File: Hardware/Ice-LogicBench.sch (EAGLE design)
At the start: 106 parts, among them IC1 S27KL0641DABHV020, IC2 S26KL128SDABHI020, IC3 USBLC6-2SC6, IC4 ICE40HX4K-BG121, IC5 FUSB302MPX, IC6 USBLC6-2SC6, J2 QWIIC_RIGHT_ANGLE, Y3 12MZ

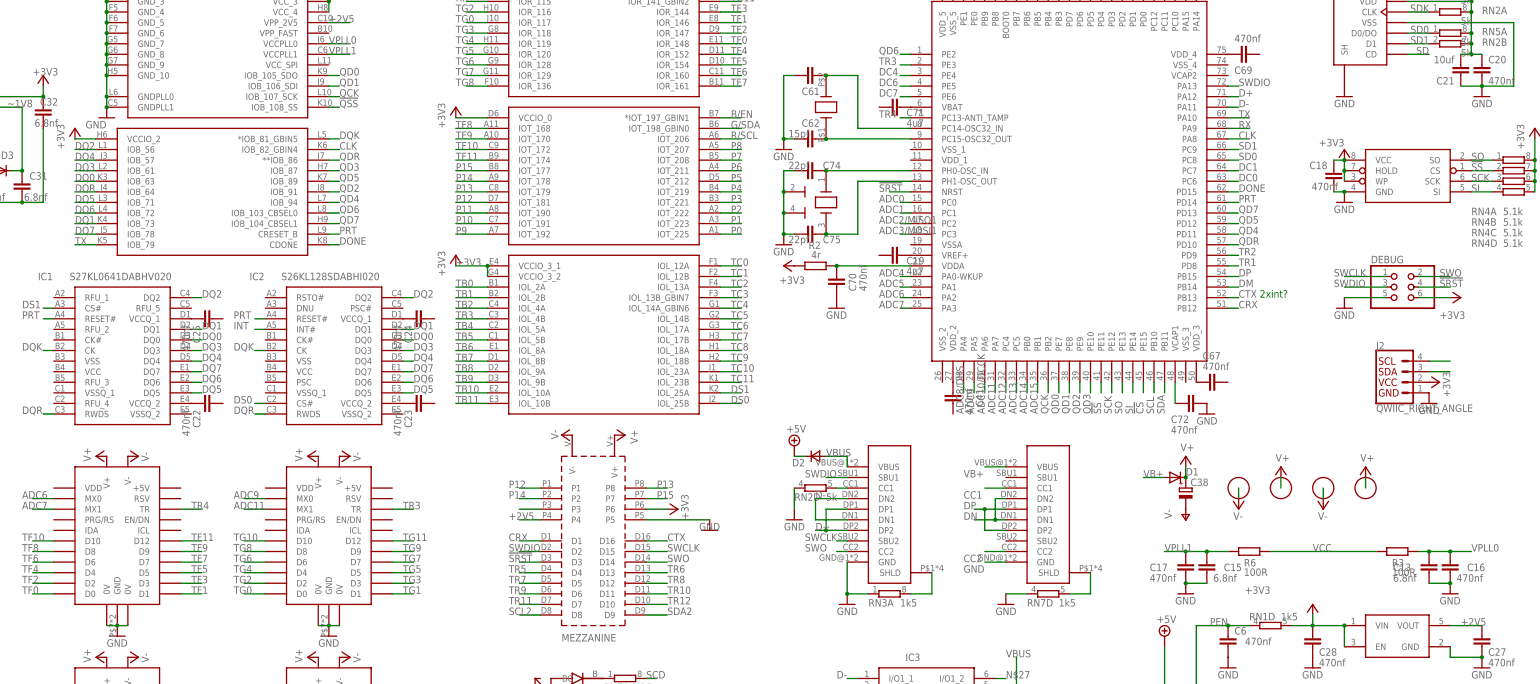
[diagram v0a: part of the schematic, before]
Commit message: Juggled some pins to improve IO frm @tnt suggestion
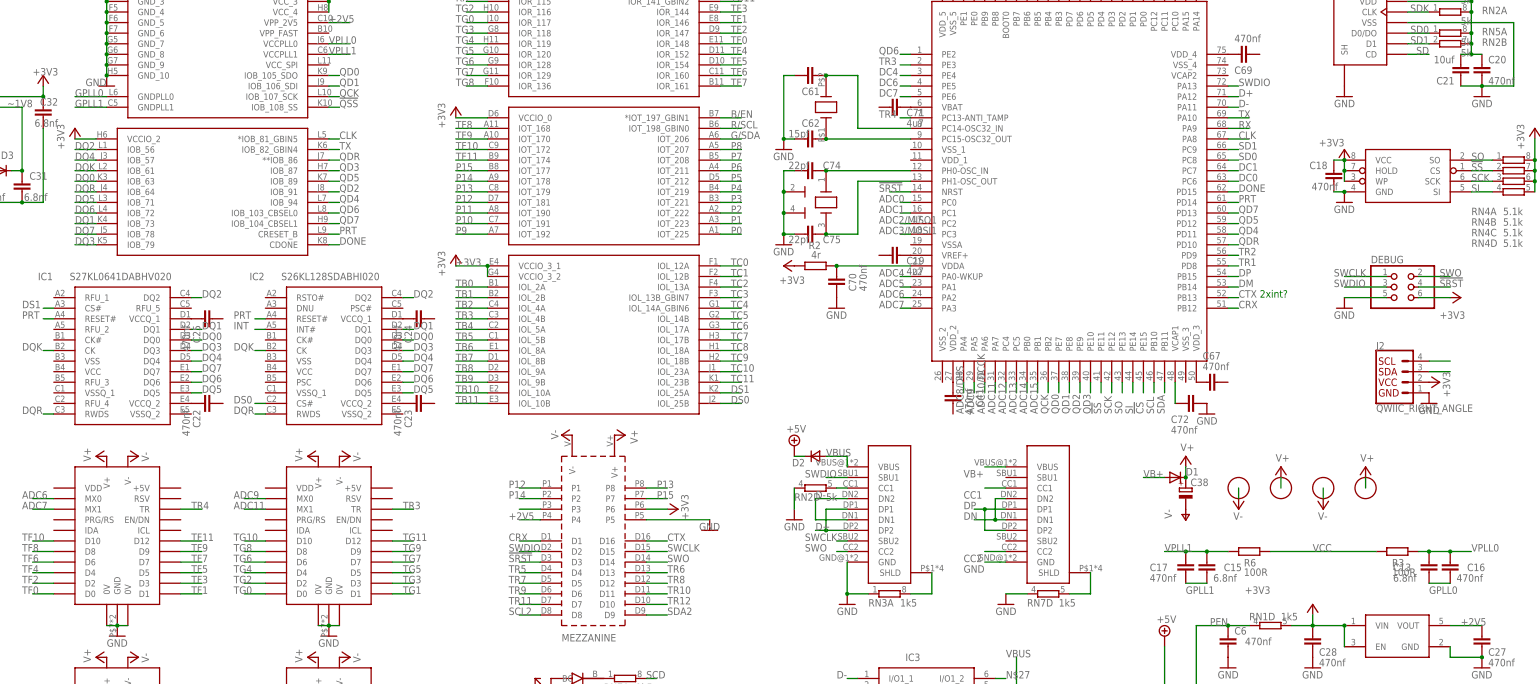
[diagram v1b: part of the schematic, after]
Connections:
- new net GPLL0: C13.1, C16.1, IC4.GNDPLL0
- new net GPLL1: C15.1, C17.1, IC4.GNDPLL1
- net CLK: now also IC4.*IOB_81_GBIN5; no longer IC4.IOB_82_GBIN4
- net DQ3: now also IC4.IOB_79; no longer IC4.IOB_61
- net DQK: now also IC4.IOB_61; no longer IC4.*IOB_81_GBIN5
- net G/SDA: now also IC4.IOT_206; no longer IC4.IOT_198_GBIN0
- net GND: no longer C13.1, C15.1, C16.1, C17.1, IC4.GNDPLL0, IC4.GNDPLL1
- net R/SCL: now also IC4.IOT_198_GBIN0; no longer IC4.IOT_206
- net TX: now also IC4.IOB_82_GBIN4; no longer IC4.IOB_79
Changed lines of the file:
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@@
 <part name="C13" library="rcl" deviceset="C-EU" device="C0402" value="6.8nf"/>
 <part name="C15" library="rcl" deviceset="C-EU" device="C0402" value="6.8nf"/>
-<part name="GND14" library="SparkFun-Aesthetics" deviceset="GND" device=""/>
-<part name="GND15" library="SparkFun-Aesthetics" deviceset="GND" device=""/>
 <part name="C16" library="rcl" deviceset="C-EU" device="C0402" value="470nf"/>
 <part name="C17" library="rcl" deviceset="C-EU" device="C0402" value="470nf"/>
@@
 <attribute name="VALUE" x="-119.38" y="35.56" size="1.778" layer="96"/>
 </instance>
-<instance part="GND7" gate="1" x="-86.36" y="172.72" smashed="yes">
-<attribute name="VALUE" x="-91.44" y="170.18" size="1.778" layer="96"/>
+<instance part="GND7" gate="1" x="-86.36" y="180.34" smashed="yes">
+<attribute name="VALUE" x="-91.44" y="180.34" size="1.778" layer="96"/>
 </instance>
 <instance part="C12" gate="G$1" x="-86.36" y="-22.86" smashed="yes" rot="MR0">
@@
 <attribute name="VALUE" x="179.324" y="63.119" size="1.778" layer="96" rot="MR180"/>
 </instance>
-<instance part="GND14" gate="1" x="236.22" y="58.42" smashed="yes">
-<attribute name="VALUE" x="233.68" y="55.88" size="1.778" layer="96"/>
-</instance>
-<instance part="GND15" gate="1" x="172.72" y="58.42" smashed="yes">
-<attribute name="VALUE" x="170.18" y="55.88" size="1.778" layer="96"/>
-</instance>
 <instance part="C16" gate="G$1" x="236.22" y="63.5" smashed="yes" rot="MR180">
 <attribute name="NAME" x="240.284" y="65.659" size="1.778" layer="95" rot="MR180"/>
@@
 </segment>
 <segment>
-<pinref part="C16" gate="G$1" pin="1"/>
-<pinref part="GND14" gate="1" pin="GND"/>
-<pinref part="C13" gate="G$1" pin="1"/>
-<wire x1="231.14" y1="60.96" x2="236.22" y2="60.96" width="0.1524" layer="91"/>
-<junction x="236.22" y="60.96"/>
-</segment>
-<segment>
-<pinref part="C17" gate="G$1" pin="1"/>
-<pinref part="GND15" gate="1" pin="GND"/>
-<pinref part="C15" gate="G$1" pin="1"/>
-<wire x1="172.72" y1="60.96" x2="177.8" y2="60.96" width="0.1524" layer="91"/>
-<junction x="172.72" y="60.96"/>
-</segment>
-<segment>
 <pinref part="SV1" gate="G$1" pin="9"/>
 <wire x1="-121.92" y1="12.7" x2="-116.84" y2="12.7" width="0.1524" layer="91"/>
@@
 </segment>
 <segment>
+<pinref part="C72" gate="G$1" pin="1"/>
+<pinref part="GND8" gate="1" pin="GND"/>
+</segment>
+<segment>
 <pinref part="IC4" gate="G$1" pin="GND_1"/>
 <pinref part="IC4" gate="G$1" pin="GND_2"/>
@@
 <wire x1="-86.36" y1="185.42" x2="-86.36" y2="182.88" width="0.1524" layer="91"/>
 <junction x="-86.36" y="185.42"/>
-<pinref part="IC4" gate="G$1" pin="GNDPLL0"/>
-<wire x1="-86.36" y1="182.88" x2="-86.36" y2="177.8" width="0.1524" layer="91"/>
-<junction x="-86.36" y="182.88"/>
-<pinref part="IC4" gate="G$1" pin="GNDPLL1"/>
-<junction x="-86.36" y="177.8"/>
-<junction x="-86.36" y="175.26"/>
-<wire x1="-86.36" y1="177.8" x2="-86.36" y2="175.26" width="0.1524" layer="91"/>
 <pinref part="GND7" gate="1" pin="GND"/>
-</segment>
-<segment>
-<pinref part="C72" gate="G$1" pin="1"/>
-<pinref part="GND8" gate="1" pin="GND"/>
+<junction x="-86.36" y="182.88"/>
 </segment>
 </net>
@@
 </segment>
 <segment>
-<pinref part="IC4" gate="G$1" pin="IOB_79"/>
-<wire x1="-88.9" y1="142.24" x2="-93.98" y2="142.24" width="0.1524" layer="91"/>
-<label x="-93.98" y="142.24" size="1.778" layer="95"/>
-</segment>
-</net>
-<net name="CLK" class="0">
-<segment>
 <pinref part="IC4" gate="G$1" pin="IOB_82_GBIN4"/>
 <wire x1="-33.02" y1="165.1" x2="-30.48" y2="165.1" width="0.1524" layer="91"/>
 <label x="-30.48" y="165.1" size="1.778" layer="95"/>
 </segment>
+</net>
+<net name="CLK" class="0">
 <segment>
 <wire x1="182.88" y1="167.64" x2="187.96" y2="167.64" width="0.1524" layer="91"/>
@@
 <pinref part="QD6" gate="G$1" pin="PA8"/>
 </segment>
+<segment>
+<pinref part="IC4" gate="G$1" pin="*IOB_81_GBIN5"/>
+<wire x1="-33.02" y1="167.64" x2="-30.48" y2="167.64" width="0.1524" layer="91"/>
+<label x="-30.48" y="167.64" size="1.778" layer="95"/>
+</segment>
 </net>
 <net name="TB0" class="0">
@@
 </segment>
 <segment>
-<pinref part="IC4" gate="G$1" pin="*IOB_81_GBIN5"/>
-<wire x1="-33.02" y1="167.64" x2="-30.48" y2="167.64" width="0.1524" layer="91"/>
-<label x="-30.48" y="167.64" size="1.778" layer="95"/>
+<pinref part="IC4" gate="G$1" pin="IOB_61"/>
+<wire x1="-88.9" y1="160.02" x2="-93.98" y2="160.02" width="0.1524" layer="91"/>
+<label x="-93.98" y="160.02" size="1.778" layer="95"/>
 </segment>
 </net>
@@
 </segment>
 <segment>
-<pinref part="IC4" gate="G$1" pin="IOB_61"/>
-<wire x1="-88.9" y1="160.02" x2="-93.98" y2="160.02" width="0.1524" layer="91"/>
-<label x="-93.98" y="160.02" size="1.778" layer="95"/>
+<pinref part="IC4" gate="G$1" pin="IOB_79"/>
+<wire x1="-88.9" y1="142.24" x2="-93.98" y2="142.24" width="0.1524" layer="91"/>
+<label x="-93.98" y="142.24" size="1.778" layer="95"/>
 </segment>
 </net>
@@
 <net name="R/SCL" class="0">
 <segment>
-<pinref part="IC4" gate="G$1" pin="IOT_206"/>
-<wire x1="60.96" y1="167.64" x2="66.04" y2="167.64" width="0.1524" layer="91"/>
-<label x="63.5" y="167.64" size="1.778" layer="95"/>
-</segment>
-<segment>
 <pinref part="RN1" gate="B" pin="2"/>
 <wire x1="43.18" y1="-2.54" x2="45.72" y2="-2.54" width="0.1524" layer="91"/>
@@
 <label x="-121.92" y="162.56" size="1.778" layer="95" rot="MR0"/>
 </segment>
-</net>
-<net name="G/SDA" class="0">
 <segment>
 <pinref part="IC4" gate="G$1" pin="IOT_198_GBIN0"/>
@@
 <label x="63.5" y="170.18" size="1.778" layer="95"/>
 </segment>
+</net>
+<net name="G/SDA" class="0">
 <segment>
 <pinref part="RN1" gate="C" pin="2"/>
@@
 <label x="-121.92" y="157.48" size="1.778" layer="95" rot="MR0"/>
 </segment>
+<segment>
+<pinref part="IC4" gate="G$1" pin="IOT_206"/>
+<wire x1="60.96" y1="167.64" x2="66.04" y2="167.64" width="0.1524" layer="91"/>
+<label x="63.5" y="167.64" size="1.778" layer="95"/>
+</segment>
 </net>
 <net name="B/EN" class="0">
@@
 </segment>
 </net>
+<net name="GPLL0" class="0">
+<segment>
+<pinref part="IC4" gate="G$1" pin="GNDPLL0"/>
+<wire x1="-86.36" y1="177.8" x2="-93.98" y2="177.8" width="0.1524" layer="91"/>
+<label x="-93.98" y="177.8" size="1.778" layer="95"/>
+</segment>
+<segment>
+<pinref part="C16" gate="G$1" pin="1"/>
+<pinref part="C13" gate="G$1" pin="1"/>
+<wire x1="231.14" y1="60.96" x2="236.22" y2="60.96" width="0.1524" layer="91"/>
+<label x="231.14" y="58.42" size="1.778" layer="95"/>
+</segment>
+</net>
+<net name="GPLL1" class="0">
+<segment>
+<pinref part="IC4" gate="G$1" pin="GNDPLL1"/>
+<wire x1="-86.36" y1="175.26" x2="-93.98" y2="175.26" width="0.1524" layer="91"/>
+<label x="-93.98" y="175.26" size="1.778" layer="95"/>
+</segment>
+<segment>
+<pinref part="C17" gate="G$1" pin="1"/>
+<pinref part="C15" gate="G$1" pin="1"/>
+<wire x1="172.72" y1="60.96" x2="177.8" y2="60.96" width="0.1524" layer="91"/>
+<label x="172.72" y="58.42" size="1.778" layer="95"/>
+</segment>
+</net>
